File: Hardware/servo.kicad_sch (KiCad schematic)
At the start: 3 parts, among them J3 ServoConnector1

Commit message: new TVS
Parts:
- removed D3: SET23A03L02, SOT95P230X109-3N, symbol iclr:SET23A03L02
- added CR1: SMBJ3V3-E3/52, CR_V3-E3/52_VIS, symbol SMBJ3V3:SMBJ3V3-E3_52
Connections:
- net GND: now also CR1.2
- net ServoPWM: now also CR1.1
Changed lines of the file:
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@@
+	(wire
+		(pts
+			(xy 129.54 86.36) (xy 133.35 86.36)
+		)
+		(stroke
+			(width 0)
+			(type default)
+		)
+	)
 	(wire
 		(pts
@@
 	(wire
 		(pts
-			(xy 124.46 63.5) (xy 132.08 63.5)
+			(xy 143.51 86.36) (xy 149.86 86.36)
 		)
 		(stroke
@@
 			(width 0)
 			(type default)
-		)
-	)
-	(hierarchical_label "ServoPWM"
-		(shape input)
-		(at 124.46 63.5 180)
-		(effects
-			(font
-				(size 1.27 1.27)
-			)
-			(justify right)
 		)
 	)
@@
 		)
 	)
+	(hierarchical_label "ServoPWM"
+		(shape input)
+		(at 149.86 86.36 0)
+		(effects
+			(font
+				(size 1.27 1.27)
+			)
+			(justify left)
+		)
+	)
 	(symbol
 		(lib_id "Connector:Conn_01x03_Pin")
@@
 	(symbol
 		(lib_id "power:GND")
-		(at 149.86 66.04 0)
-		(unit 1)
-		(exclude_from_sim no)
-		(in_bom yes)
-		(on_board yes)
-		(dnp no)
-		(fields_autoplaced yes)
-		(property "Reference" "#PWR046"
-			(at 149.86 72.39 0)
+		(at 129.54 86.36 0)
+		(unit 1)
+		(exclude_from_sim no)
+		(in_bom yes)
+		(on_board yes)
+		(dnp no)
+		(fields_autoplaced yes)
+		(property "Reference" "#PWR0132"
+			(at 129.54 92.71 0)
 			(effects
 				(font
@@
 		)
 		(property "Value" "GND"
-			(at 149.86 71.12 0)
+			(at 129.54 91.44 0)
 			(effects
 				(font
@@
 		)
 		(property "Footprint" ""
-			(at 149.86 66.04 0)
+			(at 129.54 86.36 0)
 			(effects
 				(font
@@
 		)
 		(property "Datasheet" ""
-			(at 149.86 66.04 0)
+			(at 129.54 86.36 0)
 			(effects
 				(font
@@
 		)
 		(property "Description" "Power symbol creates a global label with name \"GND\" , ground"
-			(at 149.86 66.04 0)
-			(effects
-				(font
-					(size 1.27 1.27)
-				)
-				(hide yes)
-			)
+			(at 129.54 86.36 0)
+			(effects
+				(font
+					(size 1.27 1.27)
+				)
+				(hide yes)
+			)
+		)
+		(pin "1"
+		)
+		(instances
+			(project "Reggie"
+				(path "/7db990e4-92e1-4f99-b4d2-435bbec1ba83/55ab0687-c91f-4545-a2ea-e93947dc2af8"
+					(reference "#PWR0132")
+					(unit 1)
+				)
+			)
+		)
+	)
+	(symbol
+		(lib_id "SMBJ3V3:SMBJ3V3-E3_52")
+		(at 133.35 86.36 0)
+		(unit 1)
+		(exclude_from_sim no)
+		(in_bom yes)
+		(on_board yes)
+		(dnp no)
+		(fields_autoplaced yes)
+		(property "Reference" "CR1"
+			(at 138.43 80.01 0)
+			(effects
+				(font
+					(size 1.524 1.524)
+				)
+			)
+		)
+		(property "Value" "SMBJ3V3-E3/52"
+			(at 138.43 82.55 0)
+			(effects
+				(font
+					(size 1.524 1.524)
+				)
+			)
+		)
+		(property "Footprint" "CR_V3-E3/52_VIS"
+			(at 133.35 86.36 0)
+			(effects
+				(font
+					(size 1.27 1.27)
+					(italic yes)
+				)
+				(hide yes)
+			)
+		)
+		(property "Datasheet" "https://www.vishay.com/doc?88940"
+			(at 133.35 86.36 0)
+			(effects
+				(font
+					(size 1.27 1.27)
+					(italic yes)
+				)
+				(hide yes)
+			)
+		)
+		(property "Description" ""
+			(at 133.35 86.36 0)
+			(effects
+				(font
+					(size 1.27 1.27)
+				)
+				(hide yes)
+			)
+		)
+		(pin "2"
 		)
 		(pin "1"
@@
 			(project ""
 				(path "/7db990e4-92e1-4f99-b4d2-435bbec1ba83/55ab0687-c91f-4545-a2ea-e93947dc2af8"
-					(reference "#PWR046")
-					(unit 1)
-				)
-			)
-		)
-	)
-	(symbol
-		(lib_id "iclr:SET23A03L02")
-		(at 132.08 63.5 0)
-		(unit 1)
-		(exclude_from_sim no)
-		(in_bom yes)
-		(on_board yes)
-		(dnp no)
-		(fields_autoplaced yes)
-		(property "Reference" "D3"
-			(at 140.97 55.88 0)
-			(effects
-				(font
-					(size 1.27 1.27)
-				)
-			)
-		)
-		(property "Value" "SET23A03L02"
-			(at 140.97 58.42 0)
-			(effects
-				(font
-					(size 1.27 1.27)
-				)
-			)
-		)
-		(property "Footprint" "SOT95P230X109-3N"
-			(at 156.21 158.42 0)
-			(effects
-				(font
-					(size 1.27 1.27)
-				)
-				(justify left top)
-				(hide yes)
-			)
-		)
-		(property "Datasheet" "https://www.mouser.co.uk/datasheet/3/508/1/SET23AXXL02_1.pdf"
-			(at 156.21 258.42 0)
-			(effects
-				(font
-					(size 1.27 1.27)
-				)
-				(justify left top)
-				(hide yes)
-			)
-		)
-		(property "Description" "ESD Protection Diodes / TVS Diodes TVS ESD SOIC-08 3.3V 76.8V"
-			(at 135.382 51.308 0)
-			(effects
-				(font
-					(size 1.27 1.27)
-				)
-				(hide yes)
-			)
-		)
-		(property "Height" "1.09"
-			(at 156.21 458.42 0)
-			(effects
-				(font
-					(size 1.27 1.27)
-				)
-				(justify left top)
-				(hide yes)
-			)
-		)
-		(property "Mouser Part Number" "603-SET23A03L02"
-			(at 156.21 558.42 0)
-			(effects
-				(font
-					(size 1.27 1.27)
-				)
-				(justify left top)
-				(hide yes)
-			)
-		)
-		(property "Mouser Price/Stock" "https://www.mouser.co.uk/ProductDetail/YAGEO/SET23A03L02?qs=DRkmTr78QASD5DRaK8Y6sQ%3D%3D"
-			(at 156.21 658.42 0)
-			(effects
-				(font
-					(size 1.27 1.27)
-				)
-				(justify left top)
-				(hide yes)
-			)
-		)
-		(property "Manufacturer_Name" "YAGEO"
-			(at 156.21 758.42 0)
-			(effects
-				(font
-					(size 1.27 1.27)
-				)
-				(justify left top)
-				(hide yes)
-			)
-		)
-		(property "Manufacturer_Part_Number" "SET23A03L02"
-			(at 156.21 858.42 0)
-			(effects
-				(font
-					(size 1.27 1.27)
-				)
-				(justify left top)
-				(hide yes)
-			)
-		)
-		(property "SpiceModel" ""
-			(at 160.02 46.736 0)
-			(effects
-				(font
-					(size 1.27 1.27)
-				)
-				(hide yes)
-			)
-		)
-		(property "Sim.Library" "${ICLR_HW}/spice/set23a03l02.lib"
-			(at 141.478 80.518 0)
-			(effects
-				(font
-					(size 1.27 1.27)
-				)
-				(hide yes)
-			)
-		)
-		(property "Sim.Name" "SET23A03L02_2CH"
-			(at 141.478 75.438 0)
-			(effects
-				(font
-					(size 1.27 1.27)
-				)
-				(hide yes)
-			)
-		)
-		(property "Sim.Device" "SUBCKT"
-			(at 141.478 82.55 0)
-			(effects
-				(font
-					(size 1.27 1.27)
-				)
-				(hide yes)
-			)
-		)
-		(property "Sim.Pins" "1=1 2=2 3=3"
-			(at 141.224 78.232 0)
-			(effects
-				(font
-					(size 1.27 1.27)
-				)
-				(hide yes)
-			)
-		)
-		(pin "2"
-		)
-		(pin "1"
-		)
-		(pin "3"
-		)
-		(instances
-			(project ""
-				(path "/7db990e4-92e1-4f99-b4d2-435bbec1ba83/55ab0687-c91f-4545-a2ea-e93947dc2af8"
-					(reference "D3")
-					(unit 1)
-				)
+					(reference "CR1")
+					(unit 1)
+				)

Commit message: 2nd review of schematic
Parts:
- CR1: value SMBJ3V3-E3/52 -> CPDF3V3UP-HF
- renumbered R19 to R20
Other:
- note added: "New TVS https://www.mouser.co.uk/datasheet/3/819/1/CPDF3V3UP-HF%20RevB420008.pdf"
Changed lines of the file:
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@@
+		)
+	)
+	(text "New TVS\nhttps://www.mouser.co.uk/datasheet/3/819/1/CPDF3V3UP-HF%20RevB420008.pdf "
+		(exclude_from_sim no)
+		(at 133.096 74.676 0)
+		(effects
+			(font
+				(size 1.27 1.27)
+			)
 		)
 	)
@@
 		(dnp no)
 		(fields_autoplaced yes)
-		(property "Reference" "R19"
+		(property "Reference" "R20"
 			(at 194.31 66.0399 0)
 			(effects
@@
 			(project ""
 				(path "/7db990e4-92e1-4f99-b4d2-435bbec1ba83/55ab0687-c91f-4545-a2ea-e93947dc2af8"
-					(reference "R19")
+					(reference "R20")
 					(unit 1)
 				)
@@
 		(dnp no)
 		(fields_autoplaced yes)
-		(property "Reference" "#PWR016"
+		(property "Reference" "#PWR051"
 			(at 190.5 76.2 0)
 			(effects
@@
 			(project ""
 				(path "/7db990e4-92e1-4f99-b4d2-435bbec1ba83/55ab0687-c91f-4545-a2ea-e93947dc2af8"
-					(reference "#PWR016")
+					(reference "#PWR051")
 					(unit 1)
 				)
@@
 		(dnp no)
 		(fields_autoplaced yes)
-		(property "Reference" "#PWR0132"
+		(property "Reference" "#PWR049"
 			(at 129.54 92.71 0)
 			(effects
@@
 			(project "Reggie"
 				(path "/7db990e4-92e1-4f99-b4d2-435bbec1ba83/55ab0687-c91f-4545-a2ea-e93947dc2af8"
-					(reference "#PWR0132")
+					(reference "#PWR049")
 					(unit 1)
 				)
@@
 			)
 		)
-		(property "Value" "SMBJ3V3-E3/52"
+		(property "Value" "CPDF3V3UP-HF"
 			(at 138.43 82.55 0)
 			(effects
@@
 		(dnp no)
 		(fields_autoplaced yes)
-		(property "Reference" "#PWR028"
+		(property "Reference" "#PWR050"
 			(at 185.42 76.2 0)
 			(effects
@@
 			(project ""
 				(path "/7db990e4-92e1-4f99-b4d2-435bbec1ba83/55ab0687-c91f-4545-a2ea-e93947dc2af8"
-					(reference "#PWR028")
-					(unit 1)
-				)
+					(reference "#PWR050")
+					(unit 1)
+				)

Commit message: pcb update
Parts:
- R20: footprint (none) -> Resistor_SMD:R_0402_1005Metric
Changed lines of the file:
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@@
 			)
 		)
-		(property "Footprint" ""
+		(property "Footprint" "Resistor_SMD:R_0402_1005Metric"
 			(at 189.992 67.31 90)
 			(effects

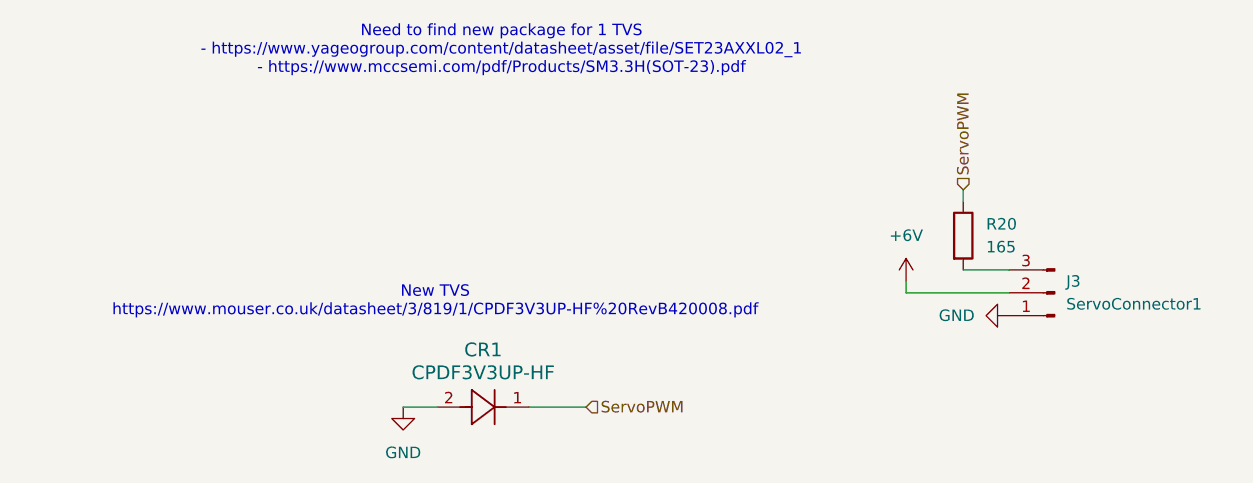
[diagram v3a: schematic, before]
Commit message: pcb and schematic update
Found all footprints including J3, pressure controller, tvs diode. PCB infrastructure update
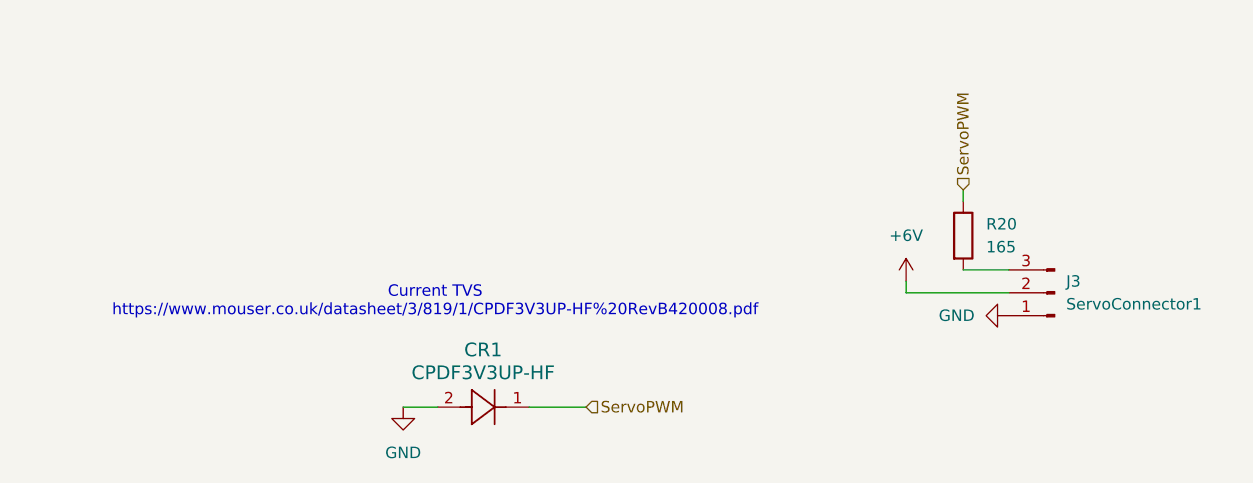
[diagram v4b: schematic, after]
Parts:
- CR1: footprint CR_V3-E3/52_VIS -> Diode_SMD:DIOM2512X90N
- J3: footprint (none) -> Connector_Molex:Molex_Nano-Fit_105313-xx03_1x03_P2.50mm_Horizontal
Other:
- note added: "Current TVS https://www.mouser.co.uk/datasheet/3/819/1/CPDF3V3UP-HF%20RevB420008.pdf"
- note removed: "Need to find new package for 1 TVS - https://www.yageogroup.com/content/datasheet/asset/file/SET23AXXL02_1 - https://www.mccsemi.com/pdf/Products/SM3.3H(SOT-23).pdf"
- note removed: "New TVS https://www.mouser.co.uk/datasheet/3/819/1/CPDF3V3UP-HF%20RevB420008.pdf"
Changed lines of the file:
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@@
 	(generator_version "9.0")
 	(paper "A4")
-	(text "Need to find new package for 1 TVS\n- https://www.yageogroup.com/content/datasheet/asset/file/SET23AXXL02_1\n- https://www.mccsemi.com/pdf/Products/SM3.3H(SOT-23).pdf"
-		(exclude_from_sim no)
-		(at 140.462 46.736 0)
-		(effects
-			(font
-				(size 1.27 1.27)
-			)
-		)
-	)
-	(text "New TVS\nhttps://www.mouser.co.uk/datasheet/3/819/1/CPDF3V3UP-HF%20RevB420008.pdf "
+	(text "Current TVS\nhttps://www.mouser.co.uk/datasheet/3/819/1/CPDF3V3UP-HF%20RevB420008.pdf "
 		(exclude_from_sim no)
 		(at 133.096 74.676 0)
@@
 			)
 		)
-		(property "Footprint" ""
+		(property "Footprint" "Connector_Molex:Molex_Nano-Fit_105313-xx03_1x03_P2.50mm_Horizontal"
 			(at 201.93 73.66 0)
 			(effects
@@
 			)
 		)
-		(property "Footprint" "CR_V3-E3/52_VIS"
+		(property "Footprint" "Diode_SMD:DIOM2512X90N"
 			(at 133.35 86.36 0)
 			(effects

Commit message: schematic changes and updated tvs footprints
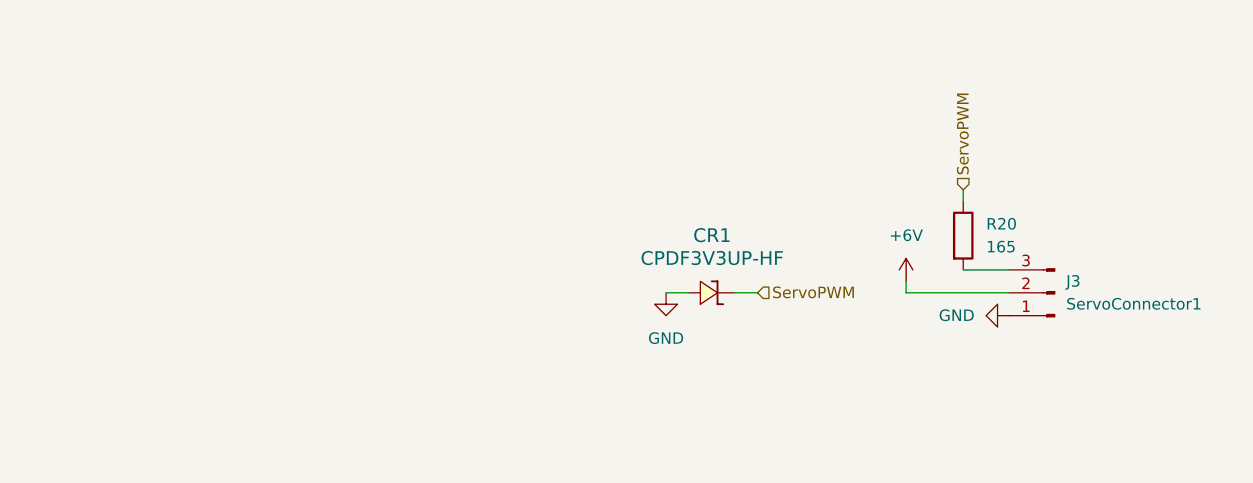
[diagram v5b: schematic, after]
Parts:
- removed CR1: CPDF3V3UP-HF, Diode_SMD:DIOM2512X90N, symbol SMBJ3V3:SMBJ3V3-E3_52
- added CR1: CPDF3V3UP-HF, iclr:CPD, symbol iclr:CPDF3V3UP-HF
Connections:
- net GND: now also CR1.1
- net ServoPWM: now also CR1.2
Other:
- note removed: "Current TVS https://www.mouser.co.uk/datasheet/3/819/1/CPDF3V3UP-HF%20RevB420008.pdf"
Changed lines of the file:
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@@
 	(generator_version "9.0")
 	(paper "A4")
-	(text "Current TVS\nhttps://www.mouser.co.uk/datasheet/3/819/1/CPDF3V3UP-HF%20RevB420008.pdf "
-		(exclude_from_sim no)
-		(at 133.096 74.676 0)
-		(effects
-			(font
-				(size 1.27 1.27)
-			)
-		)
-	)
 	(wire
 		(pts
@@
 	(wire
 		(pts
-			(xy 129.54 86.36) (xy 133.35 86.36)
+			(xy 158.75 73.66) (xy 161.29 73.66)
 		)
 		(stroke
@@
 	(wire
 		(pts
-			(xy 143.51 86.36) (xy 149.86 86.36)
+			(xy 166.37 73.66) (xy 168.91 73.66)
 		)
 		(stroke
@@
 	(hierarchical_label "ServoPWM"
 		(shape input)
-		(at 149.86 86.36 0)
+		(at 168.91 73.66 0)
 		(effects
 			(font
@@
 	(symbol
 		(lib_id "power:GND")
-		(at 129.54 86.36 0)
+		(at 158.75 73.66 0)
 		(unit 1)
 		(exclude_from_sim no)
@@
 		(fields_autoplaced yes)
 		(property "Reference" "#PWR049"
-			(at 129.54 92.71 0)
+			(at 158.75 80.01 0)
 			(effects
 				(font
@@
 		)
 		(property "Value" "GND"
-			(at 129.54 91.44 0)
+			(at 158.75 78.74 0)
 			(effects
 				(font
@@
 		)
 		(property "Footprint" ""
-			(at 129.54 86.36 0)
+			(at 158.75 73.66 0)
 			(effects
 				(font
@@
 		)
 		(property "Datasheet" ""
-			(at 129.54 86.36 0)
+			(at 158.75 73.66 0)
 			(effects
 				(font
@@
 		)
 		(property "Description" "Power symbol creates a global label with name \"GND\" , ground"
-			(at 129.54 86.36 0)
+			(at 158.75 73.66 0)
 			(effects
 				(font
@@
 	)
 	(symbol
-		(lib_id "SMBJ3V3:SMBJ3V3-E3_52")
-		(at 133.35 86.36 0)
+		(lib_id "iclr:CPDF3V3UP-HF")
+		(at 163.83 73.66 0)
 		(unit 1)
 		(exclude_from_sim no)
@@
 		(fields_autoplaced yes)
 		(property "Reference" "CR1"
-			(at 138.43 80.01 0)
+			(at 163.8808 67.31 0)
 			(effects
 				(font
@@
 		)
 		(property "Value" "CPDF3V3UP-HF"
-			(at 138.43 82.55 0)
+			(at 163.8808 69.85 0)
 			(effects
 				(font
@@
 			)
 		)
-		(property "Footprint" "Diode_SMD:DIOM2512X90N"
-			(at 133.35 86.36 0)
+		(property "Footprint" "iclr:CPD"
+			(at 170.18 82.55 0)
 			(effects
 				(font
@@
 			)
 		)
-		(property "Datasheet" "https://www.vishay.com/doc?88940"
-			(at 133.35 86.36 0)
+		(property "Datasheet" "https://www.mouser.co.uk/datasheet/3/819/1/CPDF3V3UP-HF%20RevB420008.pdf"
+			(at 165.608 86.614 0)
 			(effects
 				(font
@@
 		)
 		(property "Description" ""
-			(at 133.35 86.36 0)
-			(effects
-				(font
+			(at 163.83 73.66 0)
+			(effects
+				(font
